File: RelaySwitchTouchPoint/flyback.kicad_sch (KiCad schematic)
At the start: 28 parts, among them Q2 NMOS, T2 CST1, U2 LT3757AEDD

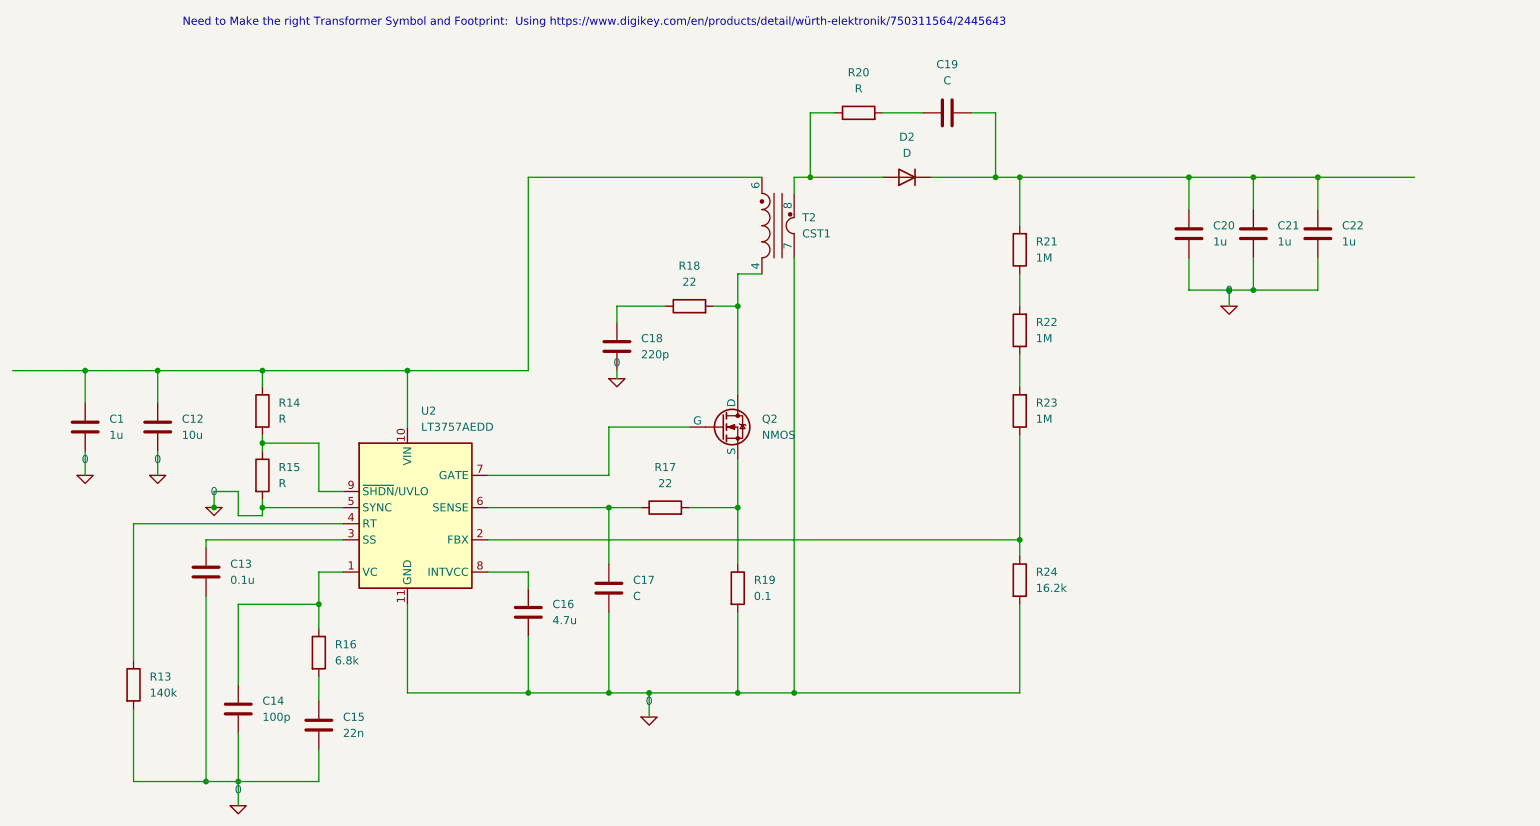
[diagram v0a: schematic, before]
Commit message: Updated Relay with proper Driver and Transformer
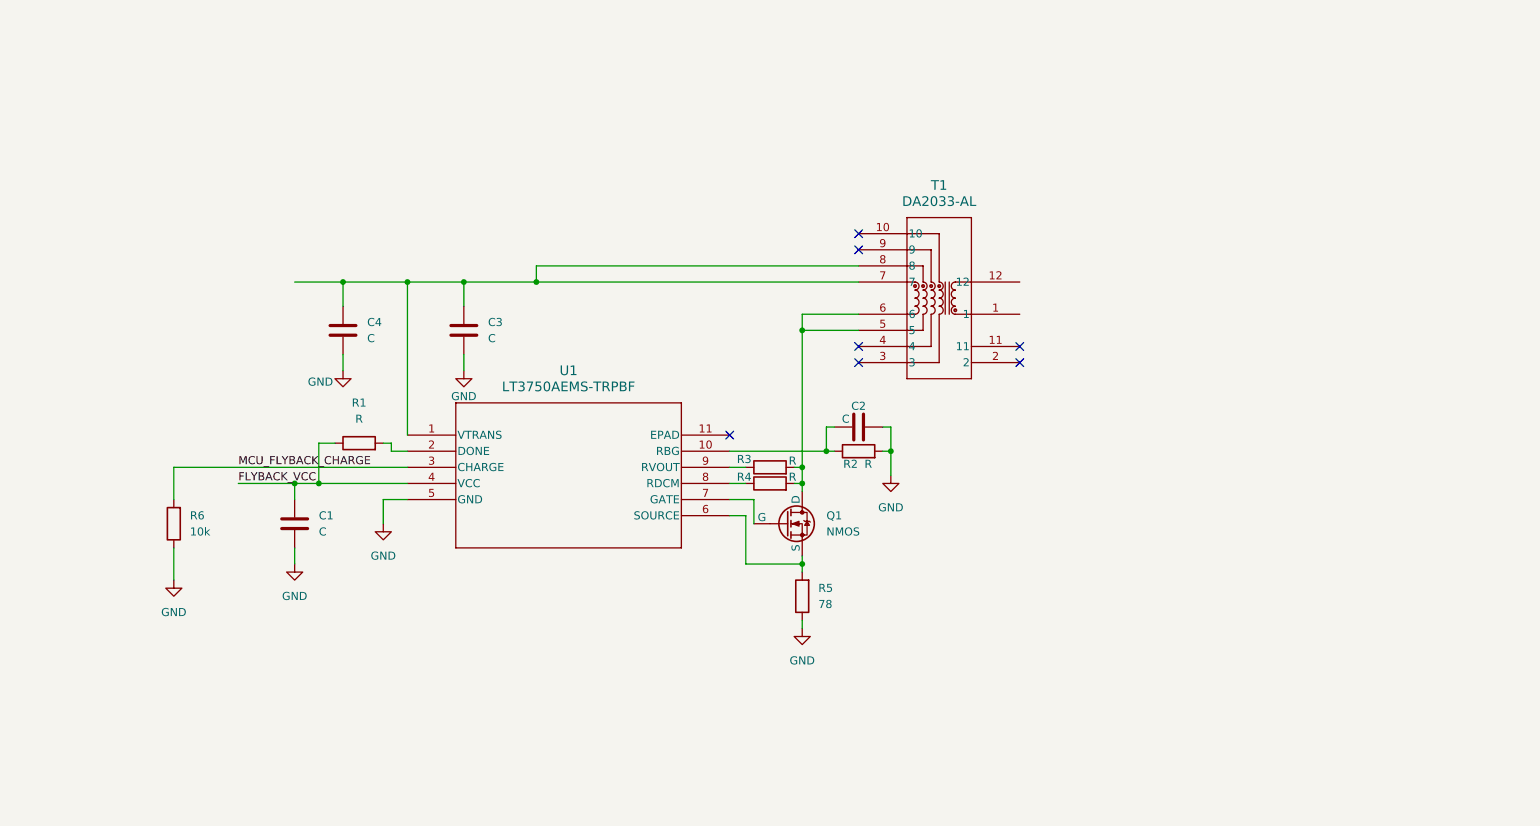
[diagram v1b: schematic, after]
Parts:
- removed C12: 10u, symbol Device:C
- removed C13: 0.1u, symbol Device:C
- removed C14: 100p, symbol Device:C
- removed C15: 22n, symbol Device:C
- removed C16: 4.7u, symbol Device:C
- removed C17, C19: C, symbol Device:C
- removed C18: 220p, symbol Device:C
- removed C20, C21, C22: 1u, symbol Device:C
- removed D2: D, symbol Device:D
- removed Q2: NMOS, symbol Simulation_SPICE:NMOS
- removed R13: 140k, symbol Device:R
- removed R14, R15, R20: R, symbol Device:R
- removed R16: 6.8k, symbol Device:R
- removed R17, R18: 22, symbol Device:R
- removed R19: 0.1, symbol Device:R
- removed R21, R22, R23: 1M, symbol Device:R
- removed R24: 16.2k, symbol Device:R
- removed T2: CST1, Transformer_SMD:Transformer_Coilcraft_CST1, symbol Transformer:CST1
- removed U2: LT3757AEDD, Package_DFN_QFN:DFN-10-1EP_3x3mm_P0.5mm_EP1.55x2.48mm, symbol Regulator_Switching:LT3757AEDD
- added C2, C3, C4: C, symbol Device:C
- added Q1: NMOS, symbol Simulation_SPICE:NMOS
- added R1, R2, R3, R4: R, symbol Device:R
- added R5: 78, symbol Device:R
- added R6: 10k, symbol Device:R
- added T1: DA2033-AL, DA2033-AL_COC, symbol DL2032:DA2033-AL
- added U1: LT3750AEMS-TRPBF, MSOP10_05-08-1664_ADI, symbol LT3750:LT3750AEMS-TRPBF
- C1: value 1u -> C
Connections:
- net FLYBACK_VCC: now reaches C1.1
- net FLYBACK_VCC: now also R1.1, U1.4 (VCC)
- net 0 renamed GND
- net GND: now also C2.2, C3.2, C4.2, R2.2, R5.1, R6.1, U1.5 (GND)
- new net: R3.1, U1.9 (RVOUT)
- new net: Q1.1 (D), R3.2, R4.2, T1.5, T1.6
- new net: Q1.3 (S), R5.2, U1.6 (SOURCE)
- new net: R4.1, U1.8 (RDCM)
- new net: C3.1, C4.1, T1.7, T1.8, U1.1 (VTRANS)
- new net: C2.1, R2.1, U1.10 (RBG)
- new net: R1.2, U1.2 (DONE)
- new net: Q1.2 (G), U1.7 (GATE)
- new net MCU_FLYBACK_CHARGE: R6.2, U1.3 (CHARGE)
- no-connect marks 0 -> 7
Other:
- note removed: "Need to Make the right Transformer Symbol and Footprint: Using https://www.digikey.com/en/products/detail/würth-elektronik/750311564/2445643"

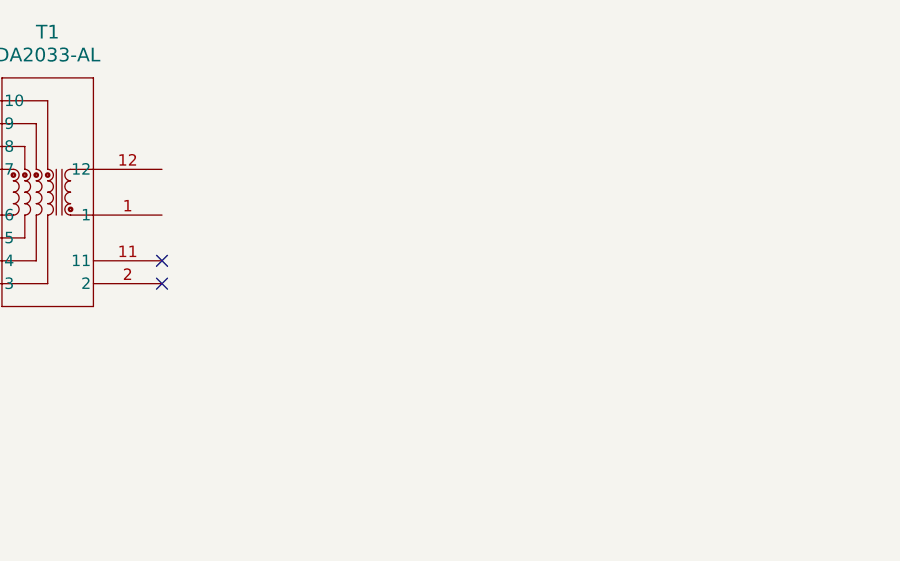
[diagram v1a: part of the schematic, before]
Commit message: Finished wiring the right side of the transformer
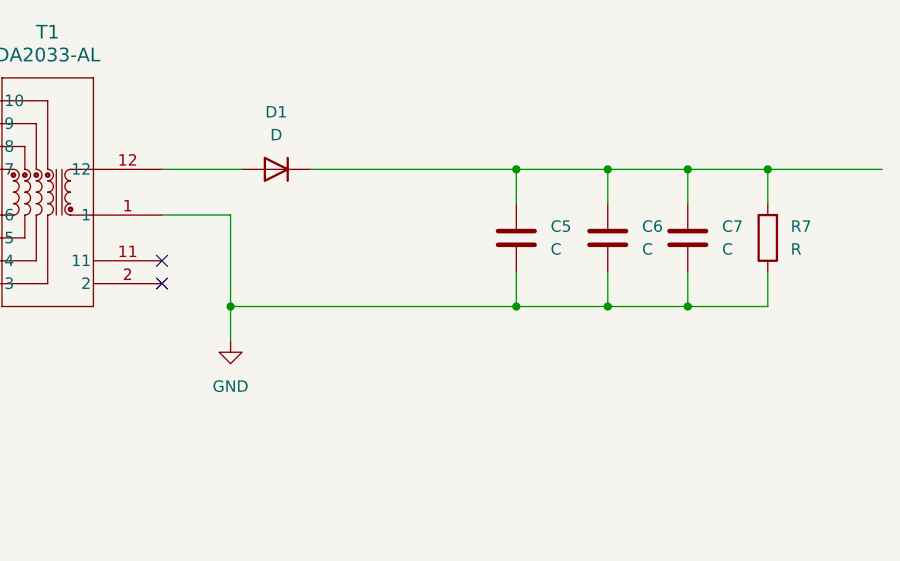
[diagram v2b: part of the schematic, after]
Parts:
- added C5, C6, C7: C, symbol Device:C
- added D1: D, symbol Device:D
- added R7: R, symbol Device:R
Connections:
- net GND: now also T1.1, C5.2, C6.2, C7.2, R7.1
- net at T1.12: now also D1.2 (A)
- new net: C5.1, C6.1, C7.1, D1.1 (K), R7.2
